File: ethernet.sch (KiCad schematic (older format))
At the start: 44 parts, among them U11 KSZ9031RNXCA, Y1 ABM8G-25.000MHZ-18-D2Y-T

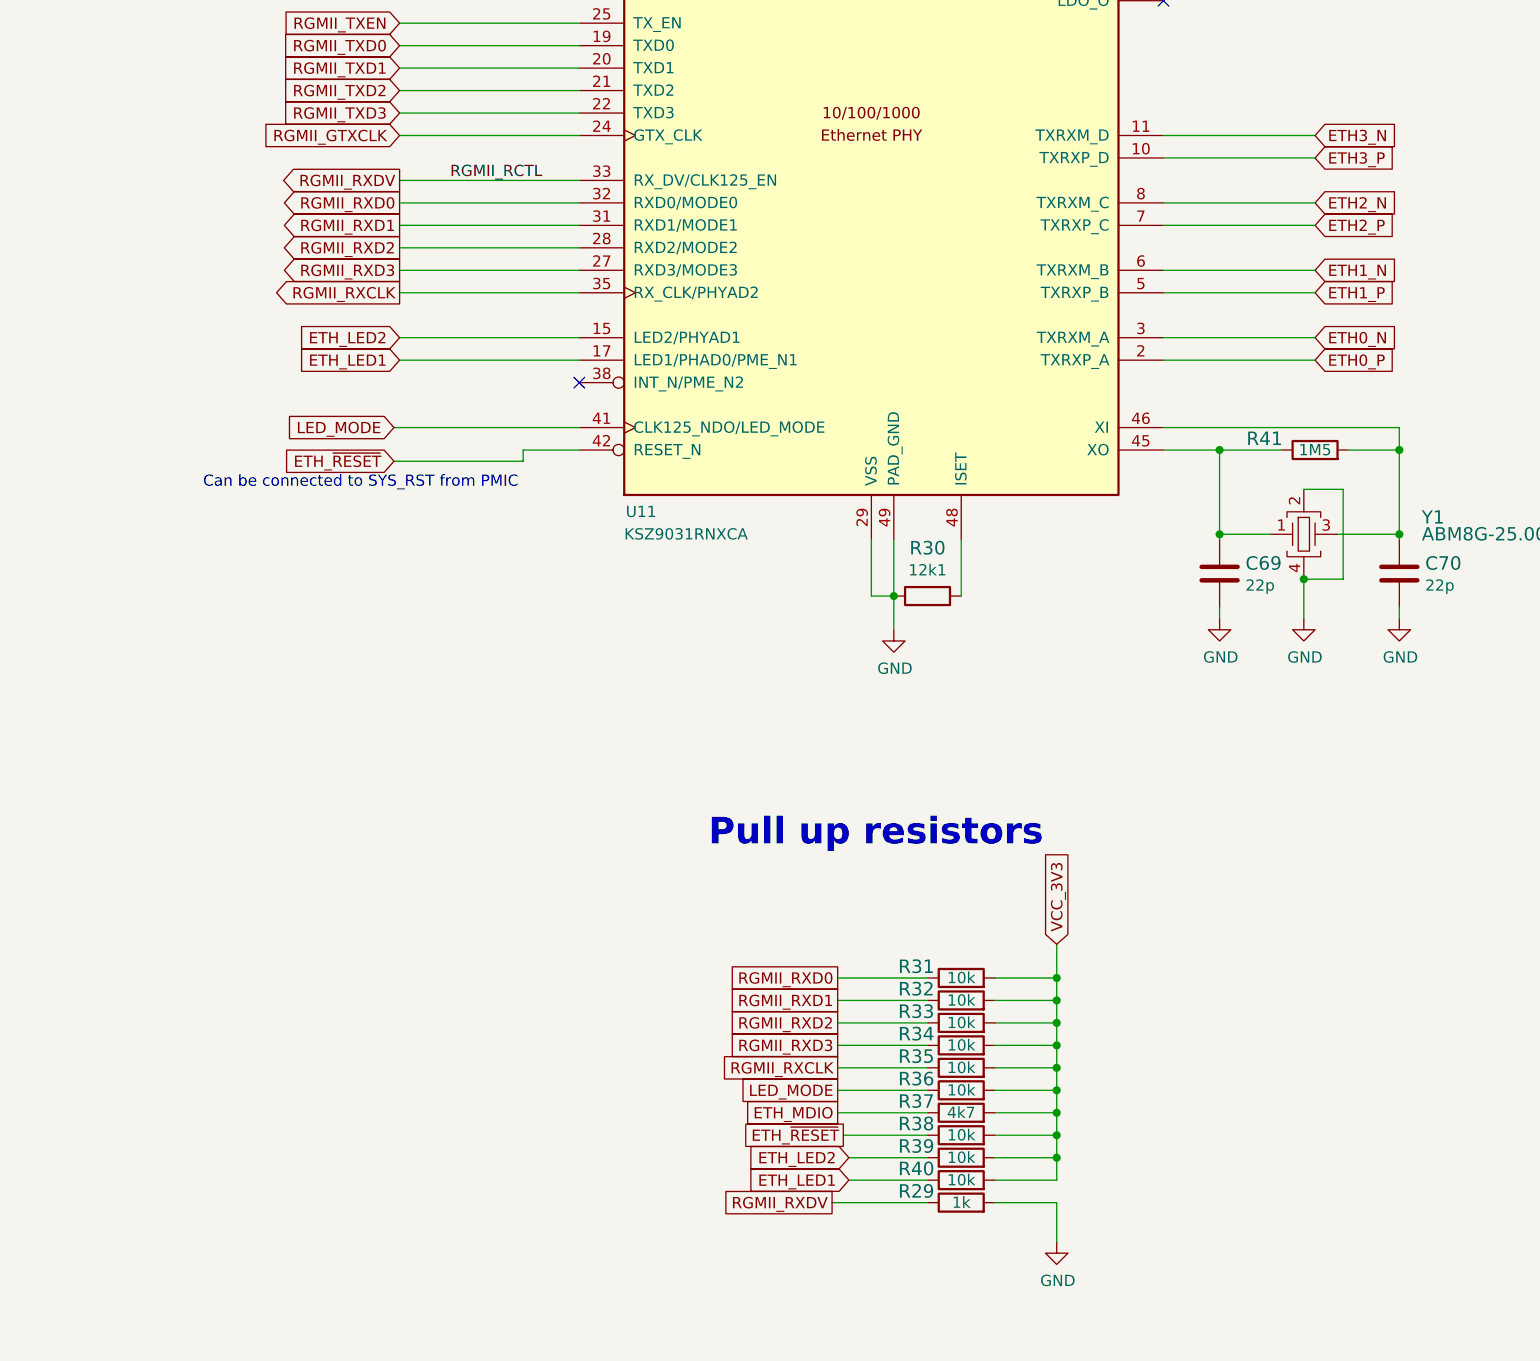
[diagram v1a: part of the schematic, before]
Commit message: Updated ethernet and interfaces.sch
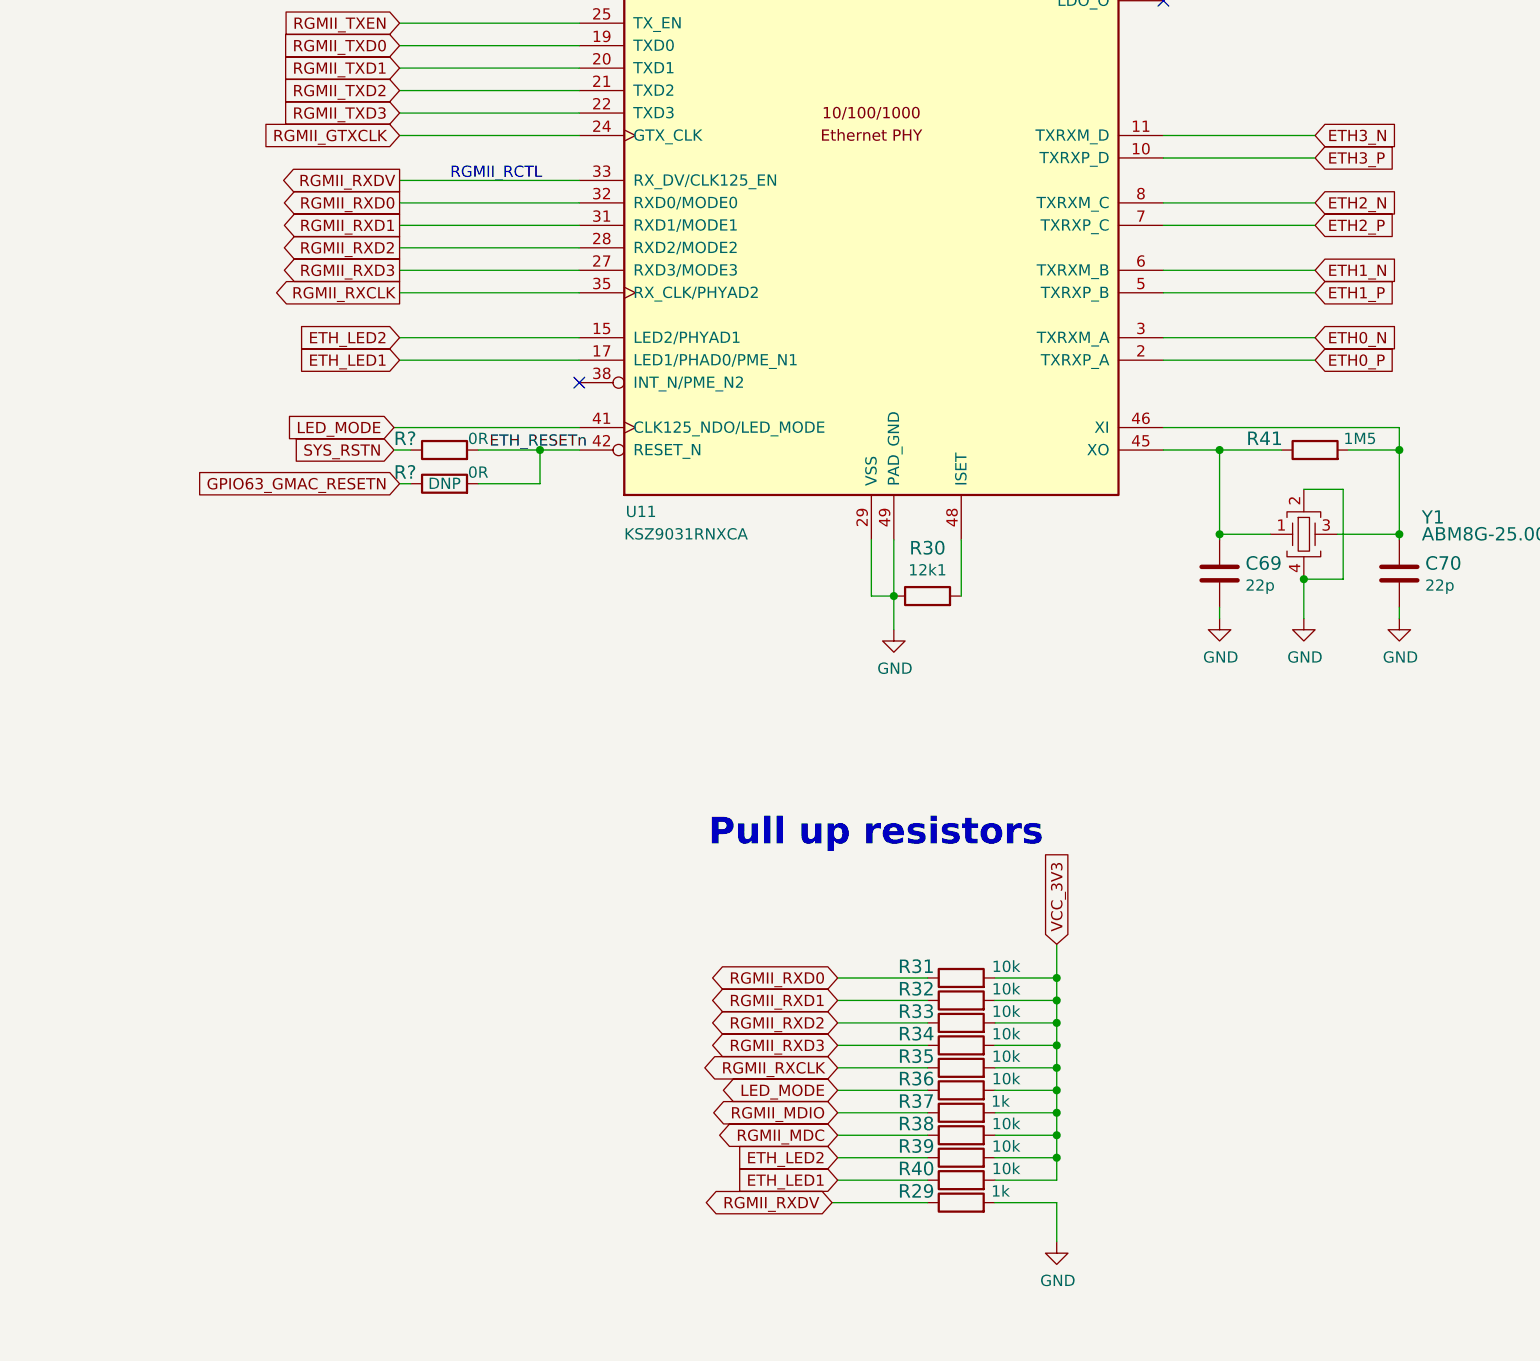
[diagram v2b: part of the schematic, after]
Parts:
- removed R37: R_4k7_0402, arvsom-footprints:0402-res, symbol arvsom:R_4k7_0402
- added R37: R_1k_0402, arvsom-footprints:0402-res, symbol arvsom:R_1k_0402
- added R? (x2): R_0R_0402, arvsom-footprints:0402-res, symbol arvsom:R_0R_0402
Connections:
- net RGMII_MDC: now also R38.1
- net RGMII_MDIO: now also R37.1
- net VCC_3V3: now also R37.2
- net ETH_~RESET renamed ETH_RESETn
- net ETH_RESETn: now also R?.2, R?.2; no longer R38.1
- new net GPIO63_GMAC_RESETN: R?.1
- new net SYS_RSTN: R?.1
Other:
- note added: "RGMII_RCTL"
- note removed: "Can be connected to SYS_RST from PMIC"
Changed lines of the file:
@@
 Comment4 ""
 $EndDescr
-Text GLabel 9825 9150 0    50   UnSpc ~ 0
+Text GLabel 9825 9150 0    50   BiDi ~ 0
 RGMII_RXDV
-Text GLabel 9850 8450 0    50   UnSpc ~ 0
+Text GLabel 9850 8450 0    50   BiDi ~ 0
 RGMII_RXD3
-Text GLabel 9850 8350 0    50   UnSpc ~ 0
+Text GLabel 9850 8350 0    50   BiDi ~ 0
 RGMII_RXD2
-Text GLabel 9850 8150 0    50   UnSpc ~ 0
+Text GLabel 9850 8150 0    50   BiDi ~ 0
 RGMII_RXD0
-Text GLabel 9850 8250 0    50   UnSpc ~ 0
+Text GLabel 9850 8250 0    50   BiDi ~ 0
 RGMII_RXD1
-Text GLabel 9850 8550 0    50   UnSpc ~ 0
+Text GLabel 9850 8550 0    50   BiDi ~ 0
 RGMII_RXCLK
 Text GLabel 10825 8000 1    50   Input ~ 0
 VCC_3V3
-Text GLabel 9850 8650 0    50   UnSpc ~ 0
+Text GLabel 9850 8650 0    50   BiDi ~ 0
 LED_MODE
-Text GLabel 9850 8750 0    50   UnSpc ~ 0
-ETH_MDIO
-Text GLabel 9875 8850 0    50   UnSpc ~ 0
-ETH_~RESET
 Wire Wire Line
 	10600 3000 10600 2775
@@
 	10400 6200 10400 6450
 NoConn ~ 11300 3800
-Text GLabel 7875 5850 0    50   Input ~ 0
-ETH_~RESET
-Wire Wire Line
-	8700 5800 8450 5800
 Wire Wire Line
 	7875 5700 8700 5700
 Text GLabel 7875 5700 0    50   Input ~ 0
 LED_MODE
-Wire Wire Line
-	8450 5800 8450 5850
-Wire Wire Line
-	8450 5850 7875 5850
 Text GLabel 7900 5000 0    50   Output ~ 0
 RGMII_RXD3
@@
 	9850 8750 10250 8750
 Wire Wire Line
-	9875 8850 10250 8850
+	9850 8850 10250 8850
 Wire Wire Line
-	9900 8950 10250 8950
+	9850 8950 10250 8950
 Wire Wire Line
-	9900 9050 10250 9050
+	9850 9050 10250 9050
 Wire Wire Line
 	10550 9050 10825 9050
@@
 F 4 "MULTICOMP" H 12175 6200 60  0001 L CNN "Manufacturer"
 F 5 "MCWR04W1504FTL" H 12175 6100 60  0001 L CNN "MPN"
-F 6 "1M5" H 11975 5800 50  0000 C CNN "Val"
+F 6 "1M5" H 12175 5850 50  0000 C CNN "Val"
 	1    11975 5800
 	1    0    0    -1
@@
 F 4 "VISHAY" H 10600 8550 60  0001 L CNN "Manufacturer"
 F 5 "CRCW040210K0FKEDHP" H 10600 8450 60  0001 L CNN "MPN"
-F 6 "10k" H 10400 8150 50  0000 C CNN "Val"
+F 6 "10k" H 10600 8200 50  0000 C CNN "Val"
 	1    10400 8150
 	1    0    0    -1
@@
 F 4 "VISHAY" H 10600 8650 60  0001 L CNN "Manufacturer"
 F 5 "CRCW040210K0FKEDHP" H 10600 8550 60  0001 L CNN "MPN"
-F 6 "10k" H 10400 8250 50  0000 C CNN "Val"
+F 6 "10k" H 10600 8300 50  0000 C CNN "Val"
 	1    10400 8250
 	1    0    0    -1
@@
 F 4 "VISHAY" H 10600 8750 60  0001 L CNN "Manufacturer"
 F 5 "CRCW040210K0FKEDHP" H 10600 8650 60  0001 L CNN "MPN"
-F 6 "10k" H 10400 8350 50  0000 C CNN "Val"
+F 6 "10k" H 10600 8400 50  0000 C CNN "Val"
 	1    10400 8350
 	1    0    0    -1
@@
 F 4 "VISHAY" H 10600 8850 60  0001 L CNN "Manufacturer"
 F 5 "CRCW040210K0FKEDHP" H 10600 8750 60  0001 L CNN "MPN"
-F 6 "10k" H 10400 8450 50  0000 C CNN "Val"
+F 6 "10k" H 10600 8500 50  0000 C CNN "Val"
 	1    10400 8450
 	1    0    0    -1
@@
 F 4 "VISHAY" H 10600 8950 60  0001 L CNN "Manufacturer"
 F 5 "CRCW040210K0FKEDHP" H 10600 8850 60  0001 L CNN "MPN"
-F 6 "10k" H 10400 8550 50  0000 C CNN "Val"
+F 6 "10k" H 10600 8600 50  0000 C CNN "Val"
 	1    10400 8550
 	1    0    0    -1
@@
 F 4 "VISHAY" H 10600 9050 60  0001 L CNN "Manufacturer"
 F 5 "CRCW040210K0FKEDHP" H 10600 8950 60  0001 L CNN "MPN"
-F 6 "10k" H 10400 8650 50  0000 C CNN "Val"
+F 6 "10k" H 10600 8700 50  0000 C CNN "Val"
 	1    10400 8650
 	1    0    0    -1
@@
 F 4 "VISHAY" H 10600 9450 60  0001 L CNN "Manufacturer"
 F 5 "CRCW040210K0FKEDHP" H 10600 9350 60  0001 L CNN "MPN"
-F 6 "10k" H 10400 9050 50  0000 C CNN "Val"
+F 6 "10k" H 10600 9100 50  0000 C CNN "Val"
 	1    10400 9050
 	1    0    0    -1
@@
 F 4 "VISHAY" H 10600 9350 60  0001 L CNN "Manufacturer"
 F 5 "CRCW040210K0FKEDHP" H 10600 9250 60  0001 L CNN "MPN"
-F 6 "10k" H 10400 8950 50  0000 C CNN "Val"
+F 6 "10k" H 10600 9000 50  0000 C CNN "Val"
 	1    10400 8950
 	1    0    0    -1
@@
 F 4 "VISHAY" H 10600 9250 60  0001 L CNN "Manufacturer"
 F 5 "CRCW040210K0FKEDHP" H 10600 9150 60  0001 L CNN "MPN"
-F 6 "10k" H 10400 8850 50  0000 C CNN "Val"
+F 6 "10k" H 10600 8900 50  0000 C CNN "Val"
 	1    10400 8850
 	1    0    0    -1
 $EndComp
-$Comp
-L arvsom:R_4k7_0402 R37
-U 1 1 609F3665
-P 10400 8750
-F 0 "R37" H 10200 8800 60  0000 C CNN
-F 1 "R_4k7_0402" H 10400 8600 60  0001 C CNN
-F 2 "arvsom-footprints:0402-res" H 10600 8950 60  0001 L CNN
-F 3 "" H 10400 8750 50  0001 C CNN
-F 4 "PANASONIC_ELECTRONIC_COMPONENTS" H 10600 9150 60  0001 L CNN "Manufacturer"
-F 5 "ERJ2GEJ472X" H 10600 9050 60  0001 L CNN "MPN"
-F 6 "4k7" H 10400 8750 50  0000 C CNN "Val"
-	1    10400 8750
-	1    0    0    -1
-$EndComp
 Wire Wire Line
 	10825 8450 10825 8550
@@
 F 4 "BOURNS" H 10600 9550 60  0001 L CNN "Manufacturer"
 F 5 "CR0402-FX-1001GLF" H 10600 9450 60  0001 L CNN "MPN"
-F 6 "1k" H 10400 9150 50  0000 C CNN "Val"
+F 6 "1k" H 10575 9200 50  0000 C CNN "Val"
 	1    10400 9150
 	1    0    0    -1
@@
 Text GLabel 7900 3600 0    50   Input ~ 0
 RGMII_MDC
-Text GLabel 9900 8950 0    50   Input ~ 0
+Text GLabel 9850 8950 0    50   Input ~ 0
 ETH_LED2
-Text GLabel 9900 9050 0    50   Input ~ 0
+Text GLabel 9850 9050 0    50   Input ~ 0
 ETH_LED1
 NoConn ~ 8700 5500
-Text Notes 7025 5975 0    50   ~ 0
-Can be connected to SYS_RST from PMIC
-Text Label 8125 4600 0    50   ~ 0
-RGMII_RCTL
 $Bitmap
 Pos 1500 10693
@@
 Wire Wire Line
 	1725 3725 2125 3725
+Text Notes 8125 4600 0    50   ~ 0
+RGMII_RCTL
+Text GLabel 7875 5800 0    50   Input ~ 0
+SYS_RSTN
+$Comp
+L arvsom:R_0R_0402 R?
+U 1 1 60990FCF
+P 8100 5800
+AR Path="/60751C8D/60990FCF" Ref="R?"  Part="1"
+AR Path="/60980C6E/60990FCF" Ref="R?"  Part="1"
+F 0 "R?" H 7925 5850 60  0000 C CNN
+F 1 "R_0R_0402" H 8100 5650 60  0001 C CNN
+F 2 "arvsom-footprints:0402-res" H 8300 6000 60  0001 L CNN
+F 3 "" H 8100 5800 50  0001 C CNN
+F 4 "PANASONIC" H 8300 6200 60  0001 L CNN "Manufacturer"
+F 5 "ERJ2GE0R00X" H 8300 6100 60  0001 L CNN "MPN"
+F 6 "0R" H 8250 5850 50  0000 C CNN "Val"
+	1    8100 5800
+	1    0    0    -1
+$EndComp
+Text GLabel 7900 5950 0    50   Input ~ 0
+GPIO63_GMAC_RESETN
+$Comp
+L arvsom:R_0R_0402 R?
+U 1 1 609C4F31
+P 8100 5950
+AR Path="/60751C8D/609C4F31" Ref="R?"  Part="1"
+AR Path="/60980C6E/609C4F31" Ref="R?"  Part="1"
+F 0 "R?" H 7925 6000 60  0000 C CNN
+F 1 "R_0R_0402" H 8100 5800 60  0001 C CNN
+F 2 "arvsom-footprints:0402-res" H 8300 6150 60  0001 L CNN
+F 3 "" H 8100 5950 50  0001 C CNN
+F 4 "PANASONIC" H 8300 6350 60  0001 L CNN "Manufacturer"
+F 5 "ERJ2GE0R00X" H 8300 6250 60  0001 L CNN "MPN"
+F 6 "0R" H 8250 6000 50  0000 C CNN "Val"
+F 7 "DNP" H 8100 5950 50  0000 C CNN "DNP"
+	1    8100 5950
+	1    0    0    -1
+$EndComp
+Wire Wire Line
+	8700 5800 8525 5800
+Wire Wire Line
+	8250 5950 8525 5950
+Wire Wire Line
+	8525 5950 8525 5800
+Connection ~ 8525 5800
+Wire Wire Line
+	8525 5800 8250 5800
+Wire Wire Line
+	7950 5800 7875 5800
+Wire Wire Line
+	7950 5950 7900 5950
+Text Label 8300 5800 0    50   ~ 0
+ETH_RESETn
+$Comp
+L arvsom:R_1k_0402 R37
+U 1 1 60A15849
+P 10400 8750
+F 0 "R37" H 10200 8800 60  0000 C CNN
+F 1 "R_1k_0402" H 10400 8600 60  0001 C CNN
+F 2 "arvsom-footprints:0402-res" H 10600 8950 60  0001 L CNN
+F 3 "" H 10400 8750 50  0001 C CNN
+F 4 "BOURNS" H 10600 9150 60  0001 L CNN "Manufacturer"
+F 5 "CR0402-FX-1001GLF" H 10600 9050 60  0001 L CNN "MPN"
+F 6 "1k" H 10575 8800 50  0000 C CNN "Val"
+	1    10400 8750
+	1    0    0    -1
+$EndComp
+Text GLabel 9850 8750 0    50   BiDi ~ 0
+RGMII_MDIO
+Text GLabel 9850 8850 0    50   BiDi ~ 0
+RGMII_MDC
 $EndSCHEMATC

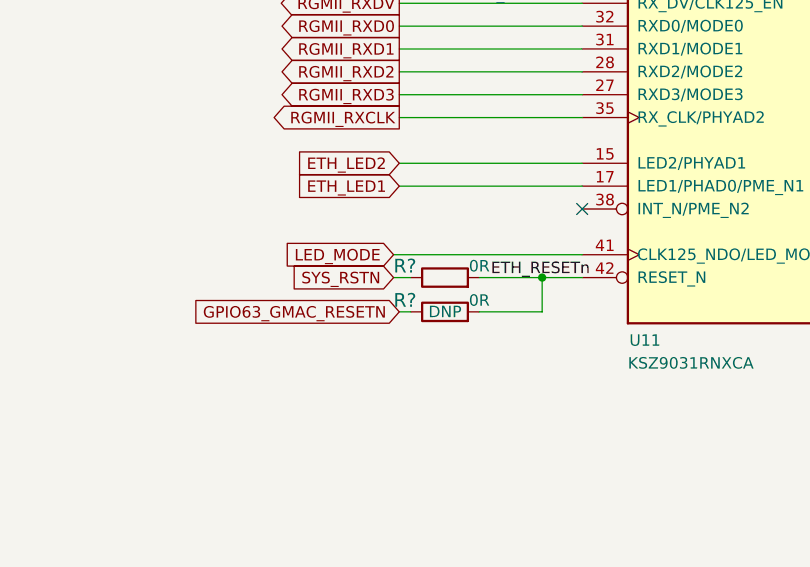
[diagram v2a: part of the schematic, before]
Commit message: Updated VIC config, added reset and crystals
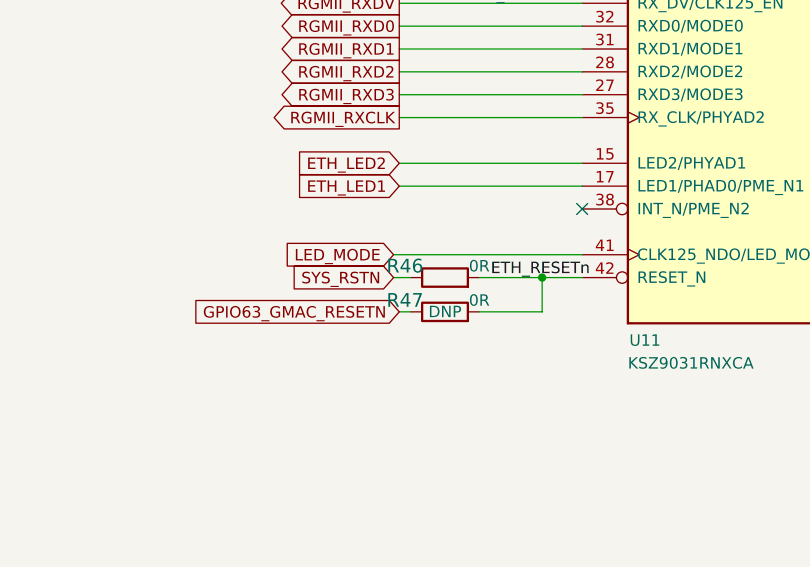
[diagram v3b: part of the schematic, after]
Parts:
- gave numbers to parts that had none: 2
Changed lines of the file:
@@
 P 8100 5800
 AR Path="/60751C8D/60990FCF" Ref="R?"  Part="1"
-AR Path="/60980C6E/60990FCF" Ref="R?"  Part="1"
-F 0 "R?" H 7925 5850 60  0000 C CNN
+AR Path="/60980C6E/60990FCF" Ref="R46"  Part="1"
+F 0 "R46" H 7925 5850 60  0000 C CNN
 F 1 "R_0R_0402" H 8100 5650 60  0001 C CNN
 F 2 "arvsom-footprints:0402-res" H 8300 6000 60  0001 L CNN
@@
 P 8100 5950
 AR Path="/60751C8D/609C4F31" Ref="R?"  Part="1"
-AR Path="/60980C6E/609C4F31" Ref="R?"  Part="1"
-F 0 "R?" H 7925 6000 60  0000 C CNN
+AR Path="/60980C6E/609C4F31" Ref="R47"  Part="1"
+F 0 "R47" H 7925 6000 60  0000 C CNN
 F 1 "R_0R_0402" H 8100 5800 60  0001 C CNN
 F 2 "arvsom-footprints:0402-res" H 8300 6150 60  0001 L CNN
